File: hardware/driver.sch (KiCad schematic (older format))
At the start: 8 parts, among them U1 74AC244, U2 74AC244, U3 74AC244, U4 ULN2803A

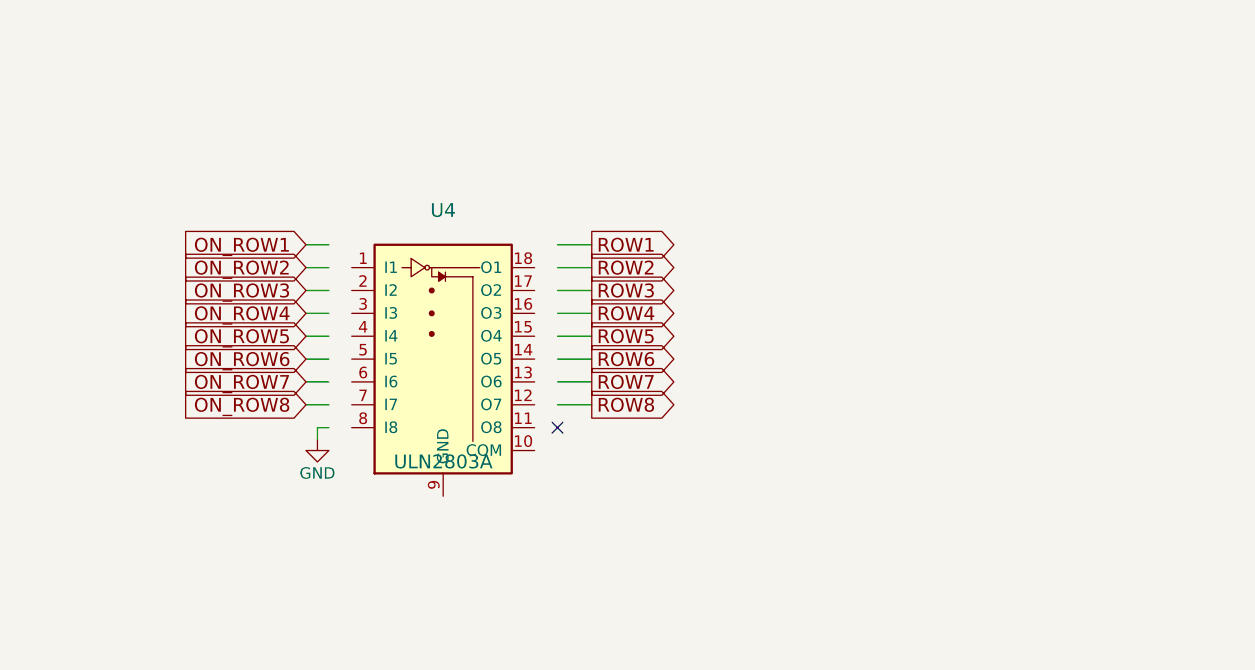
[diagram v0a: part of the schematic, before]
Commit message: LTC4417 for automatic power source switching
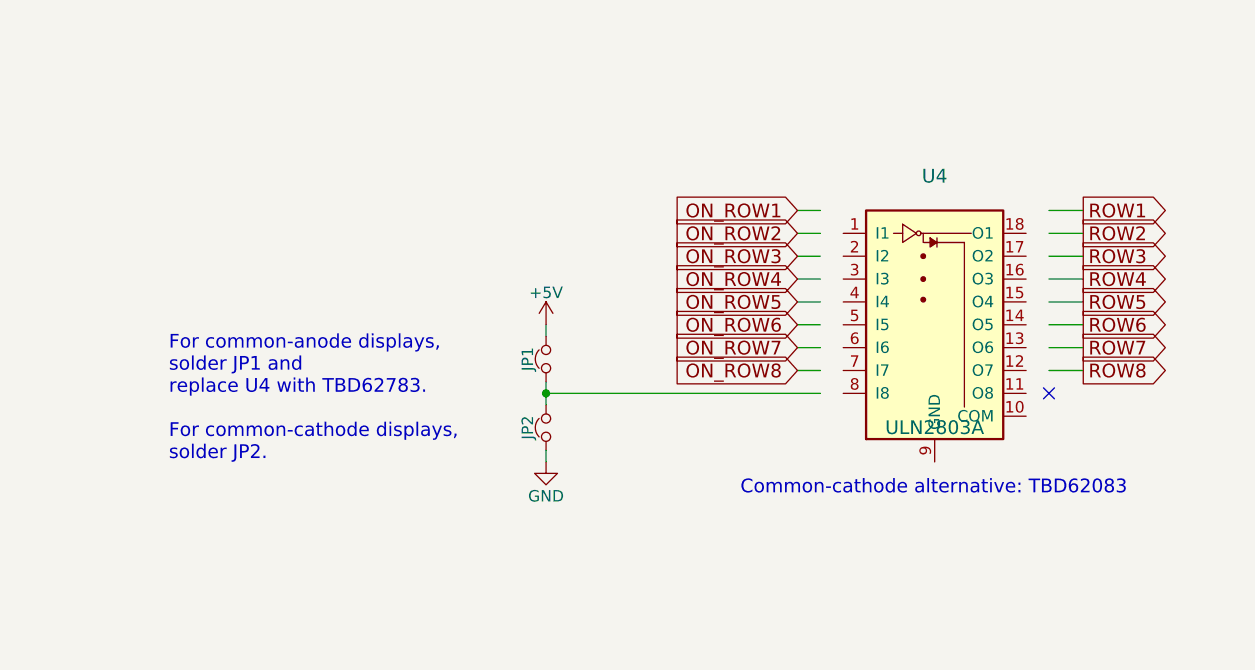
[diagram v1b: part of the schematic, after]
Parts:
- added JP1, JP2: Jumper_NC_Small, symbol Jumper_NC_Small
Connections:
- wire segments 89 -> 91
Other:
- note added: "Common-cathode alternative: TBD62083"
- note added: "For common-anode displays,\nsolder JP1 and\nreplace U4 with TBD62783.\n\nFor common-cathode displays,\nsolder JP2."
- moved on the sheet: U4

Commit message: Assign footprints
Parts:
- JP1, JP2: footprint (none) -> KiCad-Footprints:MADW__SMD-solder-bridge
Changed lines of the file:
@@
 F 0 "JP2" H 6450 4330 50  0000 C CNN
 F 1 "Jumper_NC_Small" H 6460 4190 50  0001 C CNN
-F 2 "" H 6450 4250 50  0000 C CNN
+F 2 "KiCad-Footprints:MADW__SMD-solder-bridge" H 6450 4250 50  0001 C CNN
 F 3 "" H 6450 4250 50  0000 C CNN
 	1    6450 4250
@@
 F 0 "JP1" H 6450 4030 50  0000 C CNN
 F 1 "Jumper_NC_Small" H 6460 3890 50  0001 C CNN
-F 2 "" H 6450 3950 50  0000 C CNN
+F 2 "KiCad-Footprints:MADW__SMD-solder-bridge" H 6450 3950 50  0001 C CNN
 F 3 "" H 6450 3950 50  0000 C CNN
 	1    6450 3950

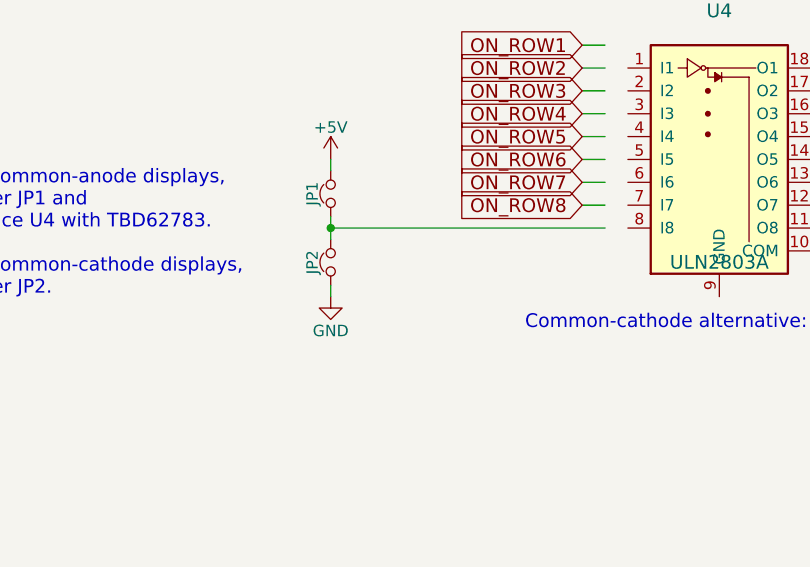
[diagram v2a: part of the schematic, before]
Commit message: Preliminary routing with LTC4417
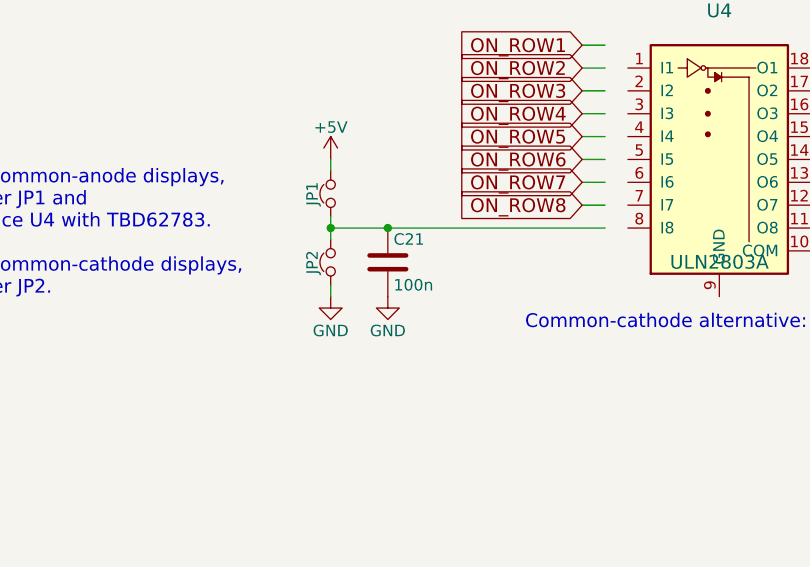
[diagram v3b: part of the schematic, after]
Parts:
- added C21: 100n, Capacitors_SMD:C_0805, symbol C
- JP1: value Jumper_NC_Small -> CA
- JP2: value Jumper_NC_Small -> CC
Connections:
- wire segments 91 -> 92
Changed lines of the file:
@@
 EESchema Schematic File Version 2
+LIBS:rgb-matrix-rescue
 LIBS:power
 LIBS:device
@@
 $EndComp
 $Comp
+L C C18
+U 1 1 584F7F50
+P 3600 6350
+F 0 "C18" H 3625 6450 50  0000 L CNN
+F 1 "100n" H 3625 6250 50  0000 L CNN
+F 2 "Capacitors_SMD:C_0805" H 3638 6200 50  0001 C CNN
+F 3 "" H 3600 6350 50  0000 C CNN
+	1    3600 6350
+	1    0    0    -1
+$EndComp
+Text Notes 7300 4550 0    60   ~ 0
+Common-cathode alternative: TBD62083
+$Comp
+L +5V #PWR09
+U 1 1 5874F556
+P 6450 3800
+F 0 "#PWR09" H 6450 3650 50  0001 C CNN
+F 1 "+5V" H 6450 3940 50  0000 C CNN
+F 2 "" H 6450 3800 50  0000 C CNN
+F 3 "" H 6450 3800 50  0000 C CNN
+	1    6450 3800
+	1    0    0    -1
+$EndComp
+Text Notes 4800 4400 0    60   ~ 0
+For common-anode displays,\nsolder JP1 and\nreplace U4 with TBD62783.\n\nFor common-cathode displays,\nsolder JP2.
+$Comp
 L C C16
 U 1 1 584F7B9B
@@
 $EndComp
 $Comp
-L C C18
-U 1 1 584F7F50
-P 3600 6350
-F 0 "C18" H 3625 6450 50  0000 L CNN
-F 1 "100n" H 3625 6250 50  0000 L CNN
-F 2 "Capacitors_SMD:C_0805" H 3638 6200 50  0001 C CNN
-F 3 "" H 3600 6350 50  0000 C CNN
-	1    3600 6350
-	1    0    0    -1
-$EndComp
-Text Notes 7300 4550 0    60   ~ 0
-Common-cathode alternative: TBD62083
+L C C21
+U 1 1 58783112
+P 6700 4250
+F 0 "C21" H 6725 4350 50  0000 L CNN
+F 1 "100n" H 6725 4150 50  0000 L CNN
+F 2 "Capacitors_SMD:C_0805" H 6738 4100 50  0001 C CNN
+F 3 "" H 6700 4250 50  0000 C CNN
+	1    6700 4250
+	1    0    0    -1
+$EndComp
+$Comp
+L GND #PWR010
+U 1 1 587832B7
+P 6700 4400
+F 0 "#PWR010" H 6700 4150 50  0001 C CNN
+F 1 "GND" H 6700 4250 50  0000 C CNN
+F 2 "" H 6700 4400 50  0000 C CNN
+F 3 "" H 6700 4400 50  0000 C CNN
+	1    6700 4400
+	1    0    0    -1
+$EndComp
 Wire Wire Line
 	3400 2700 3450 2700
@@
 Wire Wire Line
 	8800 3900 8650 3900
-Wire Wire Line
-	6450 4100 7650 4100
 Wire Wire Line
 	7550 3300 7650 3300
@@
 	3450 6500 3600 6500
 Connection ~ 3450 6500
-$Comp
-L +5V #PWR09
-U 1 1 5874F556
-P 6450 3800
-F 0 "#PWR09" H 6450 3650 50  0001 C CNN
-F 1 "+5V" H 6450 3940 50  0000 C CNN
-F 2 "" H 6450 3800 50  0000 C CNN
-F 3 "" H 6450 3800 50  0000 C CNN
-	1    6450 3800
-	1    0    0    -1
-$EndComp
 Wire Wire Line
 	6450 4350 6450 4400
 Wire Wire Line
 	6450 3800 6450 3850
-Text Notes 4800 4400 0    60   ~ 0
-For common-anode displays,\nsolder JP1 and\nreplace U4 with TBD62783.\n\nFor common-cathode displays,\nsolder JP2.
+Wire Wire Line
+	6700 4100 6700 4100
+Connection ~ 6700 4100
+Connection ~ 6450 4100
+Wire Wire Line
+	6450 4050 6450 4150
+Wire Wire Line
+	6450 4100 7650 4100
+$Comp
+L Jumper_NC_Small JP1
+U 1 1 58750A6A
+P 6450 3950
+F 0 "JP1" H 6450 4030 50  0000 C CNN
+F 1 "CA" H 6460 3890 50  0001 C CNN
+F 2 "KiCad-Footprints:MADW__SMD-solder-bridge" H 6450 3950 50  0001 C CNN
+F 3 "" H 6450 3950 50  0000 C CNN
+	1    6450 3950
+	0    -1   -1   0
+$EndComp
 $Comp
 L Jumper_NC_Small JP2
@@
 P 6450 4250
 F 0 "JP2" H 6450 4330 50  0000 C CNN
-F 1 "Jumper_NC_Small" H 6460 4190 50  0001 C CNN
+F 1 "CC" H 6460 4190 50  0001 C CNN
 F 2 "KiCad-Footprints:MADW__SMD-solder-bridge" H 6450 4250 50  0001 C CNN
 F 3 "" H 6450 4250 50  0000 C CNN
@@
 	0    -1   -1   0
 $EndComp
-Wire Wire Line
-	6450 4050 6450 4150
-$Comp
-L Jumper_NC_Small JP1
-U 1 1 58750A6A
-P 6450 3950
-F 0 "JP1" H 6450 4030 50  0000 C CNN
-F 1 "Jumper_NC_Small" H 6460 3890 50  0001 C CNN
-F 2 "KiCad-Footprints:MADW__SMD-solder-bridge" H 6450 3950 50  0001 C CNN
-F 3 "" H 6450 3950 50  0000 C CNN
-	1    6450 3950
-	0    -1   -1   0
-$EndComp
-Connection ~ 6450 4100
 $EndSCHEMATC

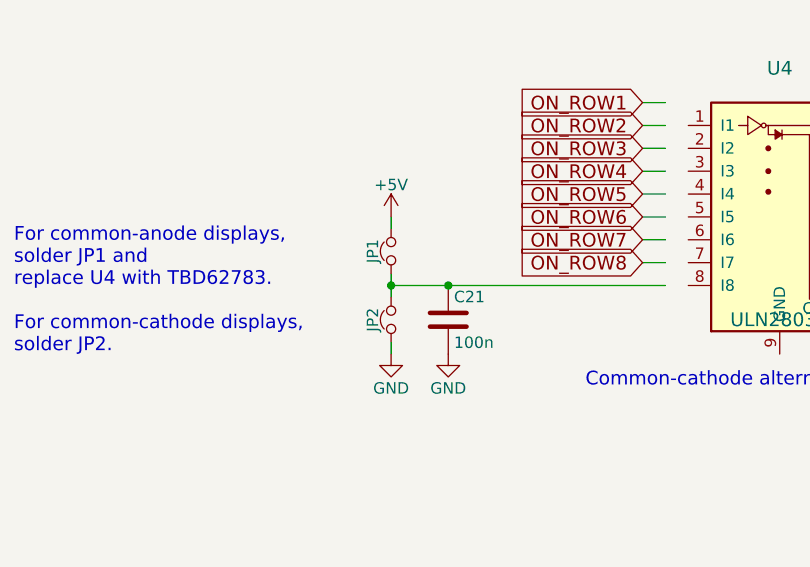
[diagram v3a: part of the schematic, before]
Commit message: Remove LTC4417, replace with solder bridges
Simply not enough space on the board!
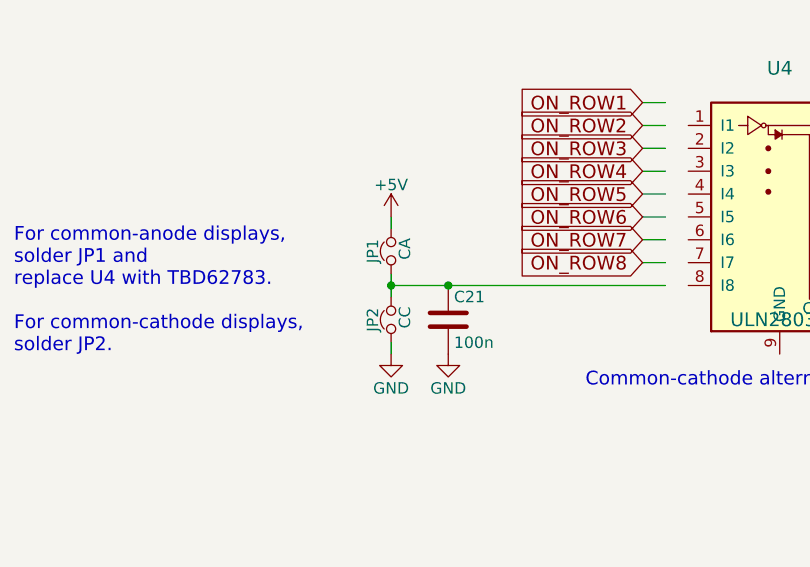
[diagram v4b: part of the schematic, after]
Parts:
- JP1, JP2: footprint KiCad-Footprints:MADW__SMD-solder-bridge -> rgb-matrix:SMD-solder-bridge-1mm
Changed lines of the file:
@@
 P 6450 3950
 F 0 "JP1" H 6450 4030 50  0000 C CNN
-F 1 "CA" H 6460 3890 50  0001 C CNN
-F 2 "KiCad-Footprints:MADW__SMD-solder-bridge" H 6450 3950 50  0001 C CNN
+F 1 "CA" H 6460 3890 50  0000 C CNN
+F 2 "rgb-matrix:SMD-solder-bridge-1mm" H 6450 3950 50  0001 C CNN
 F 3 "" H 6450 3950 50  0000 C CNN
 	1    6450 3950
@@
 P 6450 4250
 F 0 "JP2" H 6450 4330 50  0000 C CNN
-F 1 "CC" H 6460 4190 50  0001 C CNN
-F 2 "KiCad-Footprints:MADW__SMD-solder-bridge" H 6450 4250 50  0001 C CNN
+F 1 "CC" H 6460 4190 50  0000 C CNN
+F 2 "rgb-matrix:SMD-solder-bridge-1mm" H 6450 4250 50  0001 C CNN
 F 3 "" H 6450 4250 50  0000 C CNN
 	1    6450 4250

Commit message: Fix silkscreen
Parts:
- C16, C17, C18, C21: footprint Capacitors_SMD:C_0805 -> rgb-matrix:C_0805
- R25: footprint Resistors_SMD:R_0805 -> rgb-matrix:R_0805
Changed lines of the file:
@@
 F 0 "R25" V 1230 2300 50  0000 C CNN
 F 1 "10k" V 1150 2300 50  0000 C CNN
-F 2 "Resistors_SMD:R_0805" V 1080 2300 50  0001 C CNN
+F 2 "rgb-matrix:R_0805" V 1080 2300 50  0001 C CNN
 F 3 "" H 1150 2300 50  0000 C CNN
 	1    1150 2300
@@
 F 0 "C17" H 3625 4650 50  0000 L CNN
 F 1 "100n" H 3625 4450 50  0000 L CNN
-F 2 "Capacitors_SMD:C_0805" H 3638 4400 50  0001 C CNN
+F 2 "rgb-matrix:C_0805" H 3638 4400 50  0001 C CNN
 F 3 "" H 3600 4550 50  0000 C CNN
 	1    3600 4550
@@
 F 0 "C18" H 3625 6450 50  0000 L CNN
 F 1 "100n" H 3625 6250 50  0000 L CNN
-F 2 "Capacitors_SMD:C_0805" H 3638 6200 50  0001 C CNN
+F 2 "rgb-matrix:C_0805" H 3638 6200 50  0001 C CNN
 F 3 "" H 3600 6350 50  0000 C CNN
 	1    3600 6350
@@
 F 0 "C16" H 3625 2850 50  0000 L CNN
 F 1 "100n" H 3625 2650 50  0000 L CNN
-F 2 "Capacitors_SMD:C_0805" H 3638 2600 50  0001 C CNN
+F 2 "rgb-matrix:C_0805" H 3638 2600 50  0001 C CNN
 F 3 "" H 3600 2750 50  0000 C CNN
 	1    3600 2750
@@
 F 0 "C21" H 6725 4350 50  0000 L CNN
 F 1 "100n" H 6725 4150 50  0000 L CNN
-F 2 "Capacitors_SMD:C_0805" H 6738 4100 50  0001 C CNN
+F 2 "rgb-matrix:C_0805" H 6738 4100 50  0001 C CNN
 F 3 "" H 6700 4250 50  0000 C CNN
 	1    6700 4250

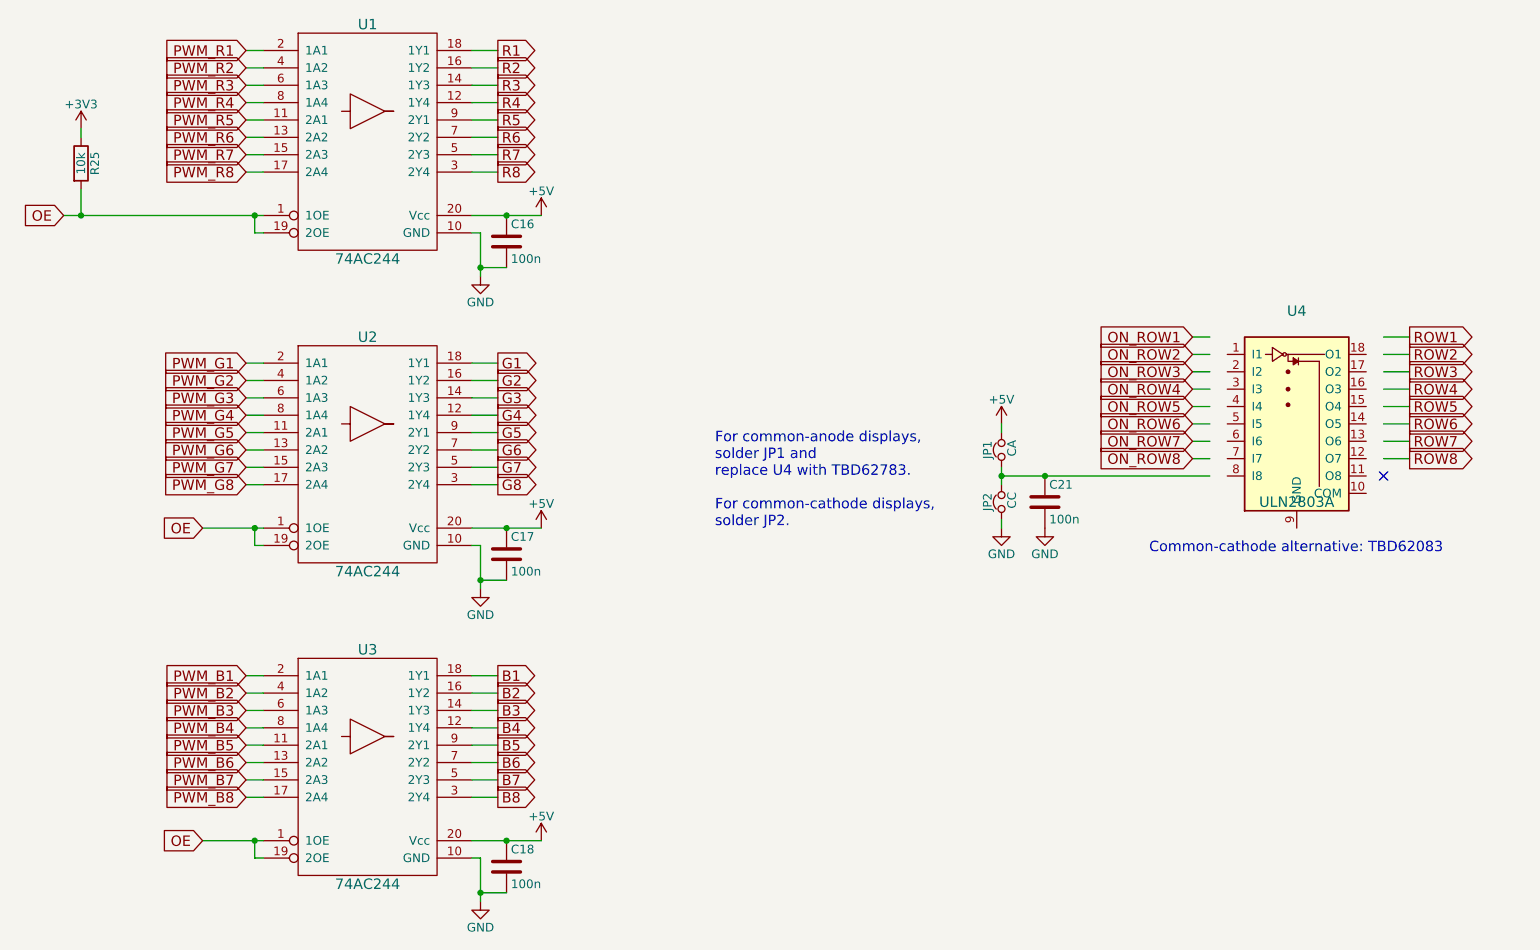
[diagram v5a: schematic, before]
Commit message: Add 2nd GND pin for more curent + minor changes
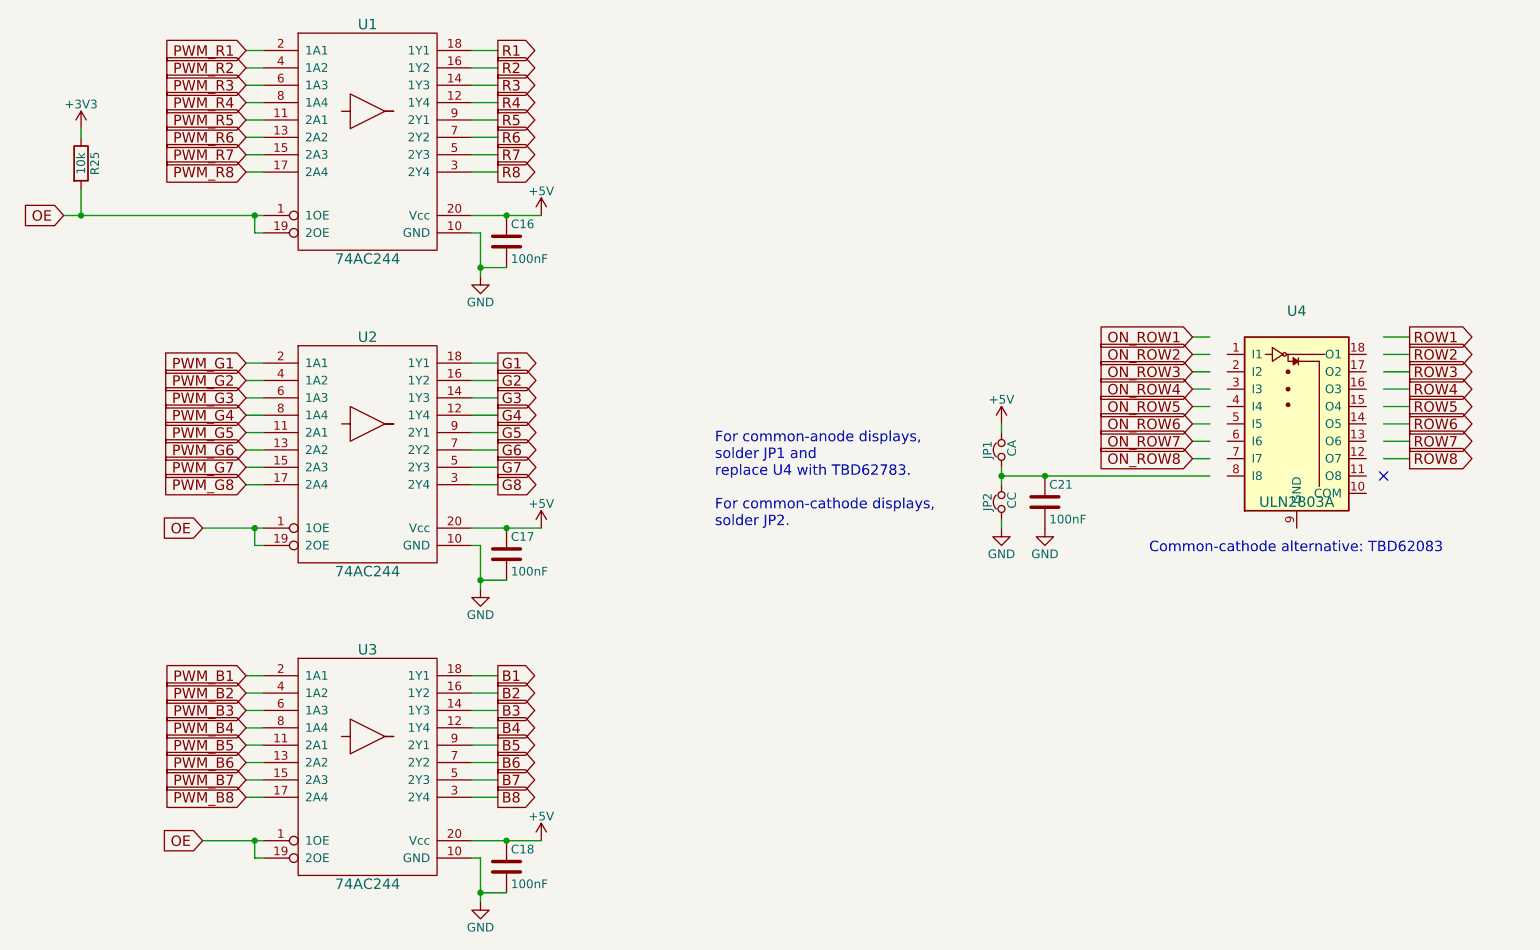
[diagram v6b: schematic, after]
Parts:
- C16, C17, C18, C21: value 100n -> 100nF
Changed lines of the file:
@@
 P 3600 4550
 F 0 "C17" H 3625 4650 50  0000 L CNN
-F 1 "100n" H 3625 4450 50  0000 L CNN
+F 1 "100nF" H 3625 4450 50  0000 L CNN
 F 2 "rgb-matrix:C_0805" H 3638 4400 50  0001 C CNN
 F 3 "" H 3600 4550 50  0000 C CNN
@@
 P 3600 6350
 F 0 "C18" H 3625 6450 50  0000 L CNN
-F 1 "100n" H 3625 6250 50  0000 L CNN
+F 1 "100nF" H 3625 6250 50  0000 L CNN
 F 2 "rgb-matrix:C_0805" H 3638 6200 50  0001 C CNN
 F 3 "" H 3600 6350 50  0000 C CNN
@@
 P 3600 2750
 F 0 "C16" H 3625 2850 50  0000 L CNN
-F 1 "100n" H 3625 2650 50  0000 L CNN
+F 1 "100nF" H 3625 2650 50  0000 L CNN
 F 2 "rgb-matrix:C_0805" H 3638 2600 50  0001 C CNN
 F 3 "" H 3600 2750 50  0000 C CNN
@@
 P 6700 4250
 F 0 "C21" H 6725 4350 50  0000 L CNN
-F 1 "100n" H 6725 4150 50  0000 L CNN
+F 1 "100nF" H 6725 4150 50  0000 L CNN
 F 2 "rgb-matrix:C_0805" H 6738 4100 50  0001 C CNN
 F 3 "" H 6700 4250 50  0000 C CNN
